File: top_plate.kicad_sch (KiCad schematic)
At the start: 36 parts, among them J35 Osc Out, J36 Conn_02x12_Odd_Even, J37 Conn_02x12_Odd_Even, J38 Conn_02x12_Odd_Even, J39 Conn_02x12_Odd_Even, J40 Conn_01x08, J41 Conn_01x08, J50 Conn_02x18_Odd_Even, J51 Conn_02x18_Odd_Even, J52 Conn_02x18_Odd_Even, J53 Conn_02x18_Odd_Even, J54 Conn_02x18_Odd_Even, J55 01x18 from bottom plate, J56 VCC, J57 VCC, J58 GND, J59 GND, J65 Conn_02x18_Odd_Even, J69 Conn_02x18_Odd_Even, J70 Conn_02x18_Odd_Even, J71 Conn_02x18_Odd_Even, J72 4040 Clk Rst, J82 Conn_02x18_Odd_Even, J83 Output, J84 Output, J87 AudioJack3, SW8 Default Clock, U10 4069

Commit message: start smd refactoring
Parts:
- C18: footprint Capacitor_THT:C_Disc_D3.0mm_W1.6mm_P2.50mm -> C_0805_2012Metric; KiLib_Generator (none) -> SMD_2terminal_chip_molded
- C19: footprint Capacitor_THT:C_Disc_D4.3mm_W1.9mm_P5.00mm -> C_0805_2012Metric; KiLib_Generator (none) -> SMD_2terminal_chip_molded
- J82: KiLib_Generator (none) -> connector/pin_header_socket
- SW8: footprint Button_Switch_THT:SW_E-Switch_EG1271_SPDT -> SW_SPDT_CK_JS102011SAQN
- U10: footprint Package_DIP:DIP-14_W7.62mm -> SOIC-14_3.9x8.7mm_P1.27mm; KiLib_Generator (none) -> package/gullwing
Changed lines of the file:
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@@
 			)
 		)
+		(property "KiLib_Generator" "connector/pin_header_socket"
+			(at 148.59 161.29 0)
+			(hide yes)
+			(show_name no)
+			(do_not_autoplace no)
+			(effects
+				(font
+					(size 1.27 1.27)
+				)
+			)
+		)
 		(pin "4"
 		)
@@
 			)
 		)
-		(property "Footprint" "Package_DIP:DIP-14_W7.62mm"
+		(property "Footprint" "SOIC-14_3.9x8.7mm_P1.27mm"
 			(at 34.29 66.04 0)
 			(hide yes)
@@
 			)
 		)
-		(property "Datasheet" "http://www.intersil.com/content/dam/Intersil/documents/cd40/cd4069ubms.pdf"
+		(property "Datasheet" ""
 			(at 34.29 66.04 0)
 			(hide yes)
@@
 			)
 		)
-		(property "Description" "Hex inverter"
+		(property "Description" ""
+			(at 34.29 66.04 0)
+			(hide yes)
+			(show_name no)
+			(do_not_autoplace no)
+			(effects
+				(font
+					(size 1.27 1.27)
+				)
+			)
+		)
+		(property "KiLib_Generator" "package/gullwing"
 			(at 34.29 66.04 0)
 			(hide yes)
@@
 			)
 		)
-		(property "Footprint" "Capacitor_THT:C_Disc_D3.0mm_W1.6mm_P2.50mm"
+		(property "Footprint" "C_0805_2012Metric"
 			(at 54.61 65.0748 0)
 			(hide yes)
@@
 			)
 		)
-		(property "Description" "Unpolarized capacitor"
+		(property "Description" ""
+			(at 50.8 66.04 0)
+			(hide yes)
+			(show_name no)
+			(do_not_autoplace no)
+			(effects
+				(font
+					(size 1.27 1.27)
+				)
+			)
+		)
+		(property "KiLib_Generator" "SMD_2terminal_chip_molded"
 			(at 50.8 66.04 0)
 			(hide yes)
@@
 			)
 		)
-		(property "Footprint" "Package_DIP:DIP-14_W7.62mm"
+		(property "Footprint" "SOIC-14_3.9x8.7mm_P1.27mm"
+			(at 69.85 66.04 0)
+			(hide yes)
+			(show_name no)
+			(do_not_autoplace no)
+			(effects
+				(font
+					(size 1.27 1.27)
+				)
+			)
+		)
+		(property "Datasheet" ""
 			(at 69.85 66.04 0)
 			(hide yes)
@@
 			)
 		)
-		(property "Datasheet" "http://www.intersil.com/content/dam/Intersil/documents/cd40/cd4069ubms.pdf"
+		(property "Description" ""
 			(at 69.85 66.04 0)
 			(hide yes)
@@
 			)
 		)
-		(property "Description" "Hex inverter"
+		(property "KiLib_Generator" "package/gullwing"
 			(at 69.85 66.04 0)
 			(hide yes)
@@
 			)
 		)
-		(property "Footprint" "Package_DIP:DIP-14_W7.62mm"
+		(property "Footprint" "SOIC-14_3.9x8.7mm_P1.27mm"
 			(at 226.06 57.15 0)
 			(hide yes)
@@
 			)
 		)
-		(property "Datasheet" "http://www.intersil.com/content/dam/Intersil/documents/cd40/cd4069ubms.pdf"
+		(property "Datasheet" ""
 			(at 226.06 57.15 0)
 			(hide yes)
@@
 			)
 		)
-		(property "Description" "Hex inverter"
+		(property "Description" ""
+			(at 226.06 57.15 0)
+			(hide yes)
+			(show_name no)
+			(do_not_autoplace no)
+			(effects
+				(font
+					(size 1.27 1.27)
+				)
+			)
+		)
+		(property "KiLib_Generator" "package/gullwing"
 			(at 226.06 57.15 0)
 			(hide yes)
@@
 			)
 		)
-		(property "Footprint" "Package_DIP:DIP-14_W7.62mm"
+		(property "Footprint" "SOIC-14_3.9x8.7mm_P1.27mm"
+			(at 35.56 101.6 0)
+			(hide yes)
+			(show_name no)
+			(do_not_autoplace no)
+			(effects
+				(font
+					(size 1.27 1.27)
+				)
+			)
+		)
+		(property "Datasheet" ""
 			(at 35.56 101.6 0)
 			(hide yes)
@@
 			)
 		)
-		(property "Datasheet" "http://www.intersil.com/content/dam/Intersil/documents/cd40/cd4069ubms.pdf"
+		(property "Description" ""
 			(at 35.56 101.6 0)
 			(hide yes)
@@
 			)
 		)
-		(property "Description" "Hex inverter"
+		(property "KiLib_Generator" "package/gullwing"
 			(at 35.56 101.6 0)
 			(hide yes)
@@
 			)
 		)
-		(property "Footprint" "Package_DIP:DIP-14_W7.62mm"
+		(property "Footprint" "SOIC-14_3.9x8.7mm_P1.27mm"
 			(at 224.79 97.79 0)
 			(hide yes)
@@
 			)
 		)
-		(property "Datasheet" "http://www.intersil.com/content/dam/Intersil/documents/cd40/cd4069ubms.pdf"
+		(property "Datasheet" ""
 			(at 224.79 97.79 0)
 			(hide yes)
@@
 			)
 		)
-		(property "Description" "Hex inverter"
+		(property "Description" ""
+			(at 224.79 97.79 0)
+			(hide yes)
+			(show_name no)
+			(do_not_autoplace no)
+			(effects
+				(font
+					(size 1.27 1.27)
+				)
+			)
+		)
+		(property "KiLib_Generator" "package/gullwing"
 			(at 224.79 97.79 0)
 			(hide yes)
@@
 			)
 		)
-		(property "Footprint" "Package_DIP:DIP-14_W7.62mm"
+		(property "Footprint" "SOIC-14_3.9x8.7mm_P1.27mm"
 			(at 148.59 43.18 0)
 			(hide yes)
@@
 			)
 		)
-		(property "Datasheet" "http://www.intersil.com/content/dam/Intersil/documents/cd40/cd4069ubms.pdf"
+		(property "Datasheet" ""
 			(at 148.59 43.18 0)
 			(hide yes)
@@
 			)
 		)
-		(property "Description" "Hex inverter"
+		(property "Description" ""
+			(at 148.59 43.18 0)
+			(hide yes)
+			(show_name no)
+			(do_not_autoplace no)
+			(effects
+				(font
+					(size 1.27 1.27)
+				)
+			)
+		)
+		(property "KiLib_Generator" "package/gullwing"
 			(at 148.59 43.18 0)
 			(hide yes)
@@
 			)
 		)
-		(property "Footprint" "Package_DIP:DIP-14_W7.62mm"
+		(property "Footprint" "SOIC-14_3.9x8.7mm_P1.27mm"
+			(at 71.12 101.6 0)
+			(hide yes)
+			(show_name no)
+			(do_not_autoplace no)
+			(effects
+				(font
+					(size 1.27 1.27)
+				)
+			)
+		)
+		(property "Datasheet" ""
 			(at 71.12 101.6 0)
 			(hide yes)
@@
 			)
 		)
-		(property "Datasheet" "http://www.intersil.com/content/dam/Intersil/documents/cd40/cd4069ubms.pdf"
+		(property "Description" ""
 			(at 71.12 101.6 0)
 			(hide yes)
@@
 			)
 		)
-		(property "Description" "Hex inverter"
+		(property "KiLib_Generator" "package/gullwing"
 			(at 71.12 101.6 0)
 			(hide yes)
@@
 			)
 		)
-		(property "Footprint" "Button_Switch_THT:SW_E-Switch_EG1271_SPDT"
+		(property "Footprint" "SW_SPDT_CK_JS102011SAQN"
 			(at 83.82 101.6 0)
 			(hide yes)
@@
 			)
 		)
-		(property "Description" "Switch, single pole double throw"
+		(property "Description" ""
 			(at 83.82 101.6 0)
 			(hide yes)
@@
 			)
 		)
-		(property "Footprint" "Capacitor_THT:C_Disc_D4.3mm_W1.9mm_P5.00mm"
+		(property "Footprint" "C_0805_2012Metric"
 			(at 55.88 100.6348 0)
 			(hide yes)
@@
 			)
 		)
-		(property "Description" "Unpolarized capacitor"
+		(property "Description" ""
+			(at 52.07 101.6 0)
+			(hide yes)
+			(show_name no)
+			(do_not_autoplace no)
+			(effects
+				(font
+					(size 1.27 1.27)
+				)
+			)
+		)
+		(property "KiLib_Generator" "SMD_2terminal_chip_molded"
 			(at 52.07 101.6 0)
 			(hide yes)

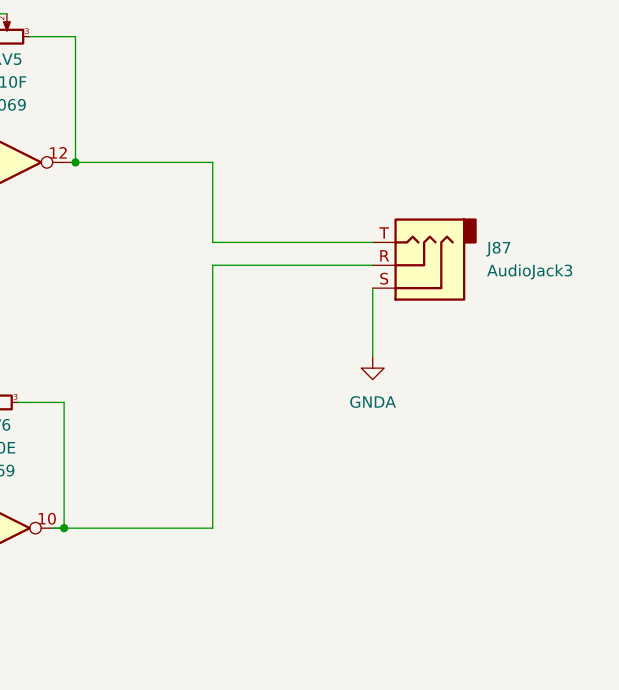
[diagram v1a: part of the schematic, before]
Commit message: clear all components, geometric constraints
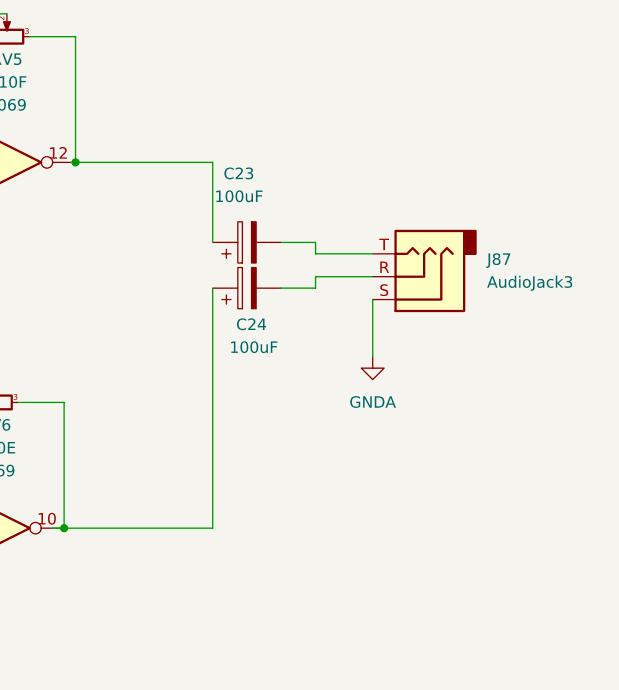
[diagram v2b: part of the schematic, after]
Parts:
- added C23, C24: 100uF, Capacitor_THT:CP_Radial_D10.0mm_P2.50mm, symbol Device:C_Polarized
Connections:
- net at RV5.3, U10.12: now also C23.1; no longer J87.T
- net at RV6.3, U10.10: now also C24.1; no longer J87.R
- new net: C24.2, J87.R
- new net: C23.2, J87.T
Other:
- moved on the sheet: J87
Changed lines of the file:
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@@
 (kicad_sch
-	(version 20260306)
+	(version 20260826)
 	(generator "eeschema")
-	(generator_version "10.0")
+	(generator_version "10.99")
 	(paper "A4")
 	(rectangle
@@
 	(wire
 		(pts
-			(xy 248.92 97.79) (xy 248.92 68.58)
+			(xy 248.92 97.79) (xy 248.92 71.12)
 		)
 		(stroke
@@
 	(wire
 		(pts
+			(xy 256.54 71.12) (xy 260.35 71.12)
+		)
+		(stroke
+			(width 0)
+			(type default)
+		)
+	)
+	(wire
+		(pts
 			(xy 214.63 57.15) (xy 218.44 57.15)
 		)
@@
 	(wire
 		(pts
+			(xy 260.35 71.12) (xy 260.35 69.85)
+		)
+		(stroke
+			(width 0)
+			(type default)
+		)
+	)
+	(wire
+		(pts
 			(xy 90.17 100.33) (xy 90.17 110.49)
 		)
@@
 	(wire
 		(pts
+			(xy 260.35 66.04) (xy 256.54 66.04)
+		)
+		(stroke
+			(width 0)
+			(type default)
+		)
+	)
+	(wire
+		(pts
 			(xy 228.6 43.18) (xy 233.68 43.18)
 		)
@@
 	(wire
 		(pts
+			(xy 260.35 69.85) (xy 266.7 69.85)
+		)
+		(stroke
+			(width 0)
+			(type default)
+		)
+	)
+	(wire
+		(pts
 			(xy 114.3 96.52) (xy 127 96.52)
 		)
@@
 	(wire
 		(pts
-			(xy 266.7 71.12) (xy 266.7 78.74)
+			(xy 266.7 72.39) (xy 266.7 78.74)
 		)
 		(stroke
@@
 	(wire
 		(pts
-			(xy 248.92 66.04) (xy 266.7 66.04)
-		)
-		(stroke
-			(width 0)
-			(type default)
-		)
-	)
-	(wire
-		(pts
 			(xy 233.68 43.18) (xy 233.68 57.15)
 		)
@@
 	(wire
 		(pts
-			(xy 248.92 68.58) (xy 266.7 68.58)
-		)
-		(stroke
-			(width 0)
-			(type default)
-		)
-	)
-	(wire
-		(pts
 			(xy 130.81 148.59) (xy 143.51 148.59)
 		)
@@
 	(wire
 		(pts
+			(xy 260.35 67.31) (xy 266.7 67.31)
+		)
+		(stroke
+			(width 0)
+			(type default)
+		)
+	)
+	(wire
+		(pts
 			(xy 29.21 171.45) (xy 41.91 171.45)
 		)
@@
 	(wire
 		(pts
+			(xy 260.35 67.31) (xy 260.35 66.04)
+		)
+		(stroke
+			(width 0)
+			(type default)
+		)
+	)
+	(wire
+		(pts
 			(xy 231.14 97.79) (xy 232.41 97.79)
 		)
@@
 	)
 	(symbol
+		(lib_id "Device:C_Polarized")
+		(at 252.73 71.12 90)
+		(unit 1)
+		(body_style 1)
+		(exclude_from_sim no)
+		(in_bom yes)
+		(on_board yes)
+		(in_pos_files yes)
+		(dnp no)
+		(property "Reference" "C24"
+			(at 253.238 75.184 90)
+			(show_name no)
+			(do_not_autoplace no)
+			(effects
+				(font
+					(size 1.27 1.27)
+				)
+			)
+		)
+		(property "Value" "100uF"
+			(at 253.492 77.724 90)
+			(show_name no)
+			(do_not_autoplace no)
+			(effects
+				(font
+					(size 1.27 1.27)
+				)
+			)
+		)
+		(property "Footprint" "Capacitor_THT:CP_Radial_D10.0mm_P2.50mm"
+			(at 256.54 70.1548 0)
+			(hide yes)
+			(show_name no)
+			(do_not_autoplace no)
+			(effects
+				(font
+					(size 1.27 1.27)
+				)
+			)
+		)
+		(property "Datasheet" ""
+			(at 252.73 71.12 0)
+			(hide yes)
+			(show_name no)
+			(do_not_autoplace no)
+			(effects
+				(font
+					(size 1.27 1.27)
+				)
+			)
+		)
+		(property "Description" "Polarized capacitor"
+			(at 252.73 71.12 0)
+			(hide yes)
+			(show_name no)
+			(do_not_autoplace no)
+			(effects
+				(font
+					(size 1.27 1.27)
+				)
+			)
+		)
+		(pin "1"
+		)
+		(pin "2"
+		)
+		(instances
+			(project "kleingorium"
+				(path "/01c1f2c1-4d06-4880-847a-9ab55552e3fd/44f3fb3f-0223-4473-937a-c9802bdd1286"
+					(reference "C24")
+					(unit 1)
+				)
+			)
+		)
+	)
+	(symbol
 		(lib_id "Connector_Generic:Conn_02x12_Odd_Even")
 		(at 119.38 106.68 0)
@@
 	(symbol
 		(lib_id "Connector_Audio:AudioJack3")
-		(at 271.78 68.58 180)
+		(at 271.78 69.85 180)
 		(unit 1)
 		(body_style 1)
@@
 		(fields_autoplaced yes)
 		(property "Reference" "J87"
-			(at 279.4 66.6749 0)
+			(at 279.4 67.9449 0)
 			(show_name no)
 			(do_not_autoplace no)
@@
 		)
 		(property "Value" "AudioJack3"
-			(at 279.4 69.2149 0)
+			(at 279.4 70.4849 0)
 			(show_name no)
 			(do_not_autoplace no)
@@
 		)
 		(property "Footprint" "Connector_Audio:Jack_3.5mm_CUI_SJ1-3523N_Horizontal"
-			(at 271.78 68.58 0)
+			(at 271.78 69.85 0)
 			(hide yes)
 			(show_name no)
@@
 		)
 		(property "Datasheet" ""
-			(at 271.78 68.58 0)
+			(at 271.78 69.85 0)
 			(hide yes)
 			(show_name no)
@@
 		)
 		(property "Description" "Audio Jack, 3 Poles (Stereo / TRS)"
-			(at 271.78 68.58 0)
+			(at 271.78 69.85 0)
 			(hide yes)
 			(show_name no)
@@
 					(unit 1)
 				)
+			)
+		)
+	)
+	(symbol
+		(lib_id "Device:C_Polarized")
+		(at 252.73 66.04 90)
+		(unit 1)
+		(body_style 1)
+		(exclude_from_sim no)
+		(in_bom yes)
+		(on_board yes)
+		(in_pos_files yes)
+		(dnp no)
+		(fields_autoplaced yes)
+		(property "Reference" "C23"
+			(at 251.841 58.42 90)
+			(show_name no)
+			(do_not_autoplace no)
+			(effects
+				(font
+					(size 1.27 1.27)
+				)
+			)
+		)
+		(property "Value" "100uF"
+			(at 251.841 60.96 90)
+			(show_name no)
+			(do_not_autoplace no)
+			(effects
+				(font
+					(size 1.27 1.27)
+				)
+			)
+		)
+		(property "Footprint" "Capacitor_THT:CP_Radial_D10.0mm_P2.50mm"
+			(at 256.54 65.0748 0)
+			(hide yes)
+			(show_name no)
+			(do_not_autoplace no)
+			(effects
+				(font
+					(size 1.27 1.27)
+				)
+			)
+		)
+		(property "Datasheet" ""
+			(at 252.73 66.04 0)
+			(hide yes)
+			(show_name no)
+			(do_not_autoplace no)
+			(effects
+				(font
+					(size 1.27 1.27)
+				)
+			)
+		)
+		(property "Description" "Polarized capacitor"
+			(at 252.73 66.04 0)
+			(hide yes)
+			(show_name no)
+			(do_not_autoplace no)
+			(effects
+				(font
+					(size 1.27 1.27)
+				)
+			)
+		)
+		(pin "1"
+		)
+		(pin "2"
+		)
+		(instances
+			(project "kleingorium"
+				(path "/01c1f2c1-4d06-4880-847a-9ab55552e3fd/44f3fb3f-0223-4473-937a-c9802bdd1286"
+					(reference "C23")
+					(unit 1)
+				)

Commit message: back to kicad 10.0
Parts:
- RV3, RV4, RV5, RV6: footprint Potentiometer_THT:Potentiometer_Alpha_RD901F-40-00D_Single_Vertical -> Potentiometer_THT:Potentiometer_Alps_RK097_Single_Horizontal
- SW8: footprint SW_SPDT_CK_JS102011SAQN -> Button_Switch_THT:SW_Slide_SPDT_Straight_CK_OS102011MS2Q
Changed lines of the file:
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@@
 (kicad_sch
-	(version 20260826)
+	(version 20260306)
 	(generator "eeschema")
-	(generator_version "10.99")
+	(generator_version "10.0")
 	(paper "A4")
 	(rectangle
@@
 			)
 		)
-		(property "Footprint" "Potentiometer_THT:Potentiometer_Alpha_RD901F-40-00D_Single_Vertical"
+		(property "Footprint" "Potentiometer_THT:Potentiometer_Alps_RK097_Single_Horizontal"
 			(at 55.88 72.39 0)
 			(hide yes)
@@
 			)
 		)
-		(property "Footprint" "Potentiometer_THT:Potentiometer_Alpha_RD901F-40-00D_Single_Vertical"
+		(property "Footprint" "Potentiometer_THT:Potentiometer_Alps_RK097_Single_Horizontal"
 			(at 224.79 83.82 0)
 			(hide yes)
@@
 			)
 		)
-		(property "Footprint" "Potentiometer_THT:Potentiometer_Alpha_RD901F-40-00D_Single_Vertical"
+		(property "Footprint" "Potentiometer_THT:Potentiometer_Alps_RK097_Single_Horizontal"
 			(at 226.06 43.18 0)
 			(hide yes)
@@
 			)
 		)
-		(property "Footprint" "Potentiometer_THT:Potentiometer_Alpha_RD901F-40-00D_Single_Vertical"
+		(property "Footprint" "Potentiometer_THT:Potentiometer_Alps_RK097_Single_Horizontal"
 			(at 57.15 107.95 0)
 			(hide yes)
@@
 			)
 		)
-		(property "Footprint" "SW_SPDT_CK_JS102011SAQN"
+		(property "Footprint" "Button_Switch_THT:SW_Slide_SPDT_Straight_CK_OS102011MS2Q"
 			(at 83.82 101.6 0)
 			(hide yes)

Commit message: wip rerouting
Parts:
- J36, J37, J38, J39: footprint Connector_PinSocket_2.54mm:PinSocket_2x12_P2.54mm_Vertical -> kleingorium:Header_2x12_P2.54mm_Vertical_SMD_FH-00369
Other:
- note added: "12x9 Matrix"
- note added: "18x24 Matrix"
- note removed: "12x8 Matrix"
- note removed: "18x20 Matrix"
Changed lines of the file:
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@@
 		)
 	)
-	(text "12x8 Matrix"
+	(text "12x9 Matrix"
 		(exclude_from_sim no)
 		(at 118.11 87.63 0)
@@
 		)
 	)
-	(text "18x20 Matrix"
+	(text "18x24 Matrix"
 		(exclude_from_sim no)
 		(at 98.298 134.366 0)
@@
 			)
 		)
-		(property "Footprint" "Connector_PinSocket_2.54mm:PinSocket_2x12_P2.54mm_Vertical"
+		(property "Footprint" "kleingorium:Header_2x12_P2.54mm_Vertical_SMD_FH-00369"
 			(at 157.48 106.68 0)
 			(hide yes)
@@
 			)
 		)
-		(property "Footprint" "Connector_PinSocket_2.54mm:PinSocket_2x12_P2.54mm_Vertical"
+		(property "Footprint" "kleingorium:Header_2x12_P2.54mm_Vertical_SMD_FH-00369"
 			(at 144.78 106.68 0)
 			(hide yes)
@@
 			)
 		)
-		(property "Footprint" "Connector_PinSocket_2.54mm:PinSocket_2x12_P2.54mm_Vertical"
+		(property "Footprint" "kleingorium:Header_2x12_P2.54mm_Vertical_SMD_FH-00369"
 			(at 119.38 106.68 0)
 			(hide yes)
@@
 			)
 		)
-		(property "Footprint" "Connector_PinSocket_2.54mm:PinSocket_2x12_P2.54mm_Vertical"
+		(property "Footprint" "kleingorium:Header_2x12_P2.54mm_Vertical_SMD_FH-00369"
 			(at 132.08 106.68 0)
 			(hide yes)

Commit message: top plate pin matrix
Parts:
- J50, J51, J52, J53, J54, J65, J82: footprint Connector_PinHeader_2.54mm:PinHeader_2x18_P2.54mm_Vertical -> kleingorium:Header_2x18_P2.54mm_Vertical_SMD_FH-00369
- J69, J70, J71: footprint Connector_PinSocket_2.54mm:PinSocket_2x18_P2.54mm_Vertical -> kleingorium:Header_2x18_P2.54mm_Vertical_SMD_FH-00369
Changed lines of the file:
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@@
 			)
 		)
-		(property "Footprint" "Connector_PinHeader_2.54mm:PinHeader_2x18_P2.54mm_Vertical"
+		(property "Footprint" "kleingorium:Header_2x18_P2.54mm_Vertical_SMD_FH-00369"
 			(at 148.59 161.29 0)
 			(hide yes)
@@
 			)
 		)
-		(property "Footprint" "Connector_PinHeader_2.54mm:PinHeader_2x18_P2.54mm_Vertical"
+		(property "Footprint" "kleingorium:Header_2x18_P2.54mm_Vertical_SMD_FH-00369"
 			(at 97.79 161.29 0)
 			(hide yes)
@@
 			)
 		)
-		(property "Footprint" "Connector_PinSocket_2.54mm:PinSocket_2x18_P2.54mm_Vertical"
+		(property "Footprint" "kleingorium:Header_2x18_P2.54mm_Vertical_SMD_FH-00369"
 			(at 135.89 161.29 0)
 			(hide yes)
@@
 			)
 		)
-		(property "Footprint" "Connector_PinHeader_2.54mm:PinHeader_2x18_P2.54mm_Vertical"
+		(property "Footprint" "kleingorium:Header_2x18_P2.54mm_Vertical_SMD_FH-00369"
 			(at 85.09 161.29 0)
 			(hide yes)
@@
 			)
 		)
-		(property "Footprint" "Connector_PinSocket_2.54mm:PinSocket_2x18_P2.54mm_Vertical"
+		(property "Footprint" "kleingorium:Header_2x18_P2.54mm_Vertical_SMD_FH-00369"
 			(at 123.19 161.29 0)
 			(hide yes)
@@
 			)
 		)
-		(property "Footprint" "Connector_PinHeader_2.54mm:PinHeader_2x18_P2.54mm_Vertical"
+		(property "Footprint" "kleingorium:Header_2x18_P2.54mm_Vertical_SMD_FH-00369"
 			(at 46.99 161.29 0)
 			(hide yes)
@@
 			)
 		)
-		(property "Footprint" "Connector_PinHeader_2.54mm:PinHeader_2x18_P2.54mm_Vertical"
+		(property "Footprint" "kleingorium:Header_2x18_P2.54mm_Vertical_SMD_FH-00369"
 			(at 34.29 161.29 0)
 			(hide yes)
@@
 			)
 		)
-		(property "Footprint" "Connector_PinSocket_2.54mm:PinSocket_2x18_P2.54mm_Vertical"
+		(property "Footprint" "kleingorium:Header_2x18_P2.54mm_Vertical_SMD_FH-00369"
 			(at 110.49 161.29 0)
 			(hide yes)
@@
 			)
 		)
-		(property "Footprint" "Connector_PinHeader_2.54mm:PinHeader_2x18_P2.54mm_Vertical"
+		(property "Footprint" "kleingorium:Header_2x18_P2.54mm_Vertical_SMD_FH-00369"
 			(at 72.39 161.29 0)
 			(hide yes)
@@
 			)
 		)
-		(property "Footprint" "Connector_PinHeader_2.54mm:PinHeader_2x18_P2.54mm_Vertical"
+		(property "Footprint" "kleingorium:Header_2x18_P2.54mm_Vertical_SMD_FH-00369"
 			(at 59.69 161.29 0)
 			(hide yes)
